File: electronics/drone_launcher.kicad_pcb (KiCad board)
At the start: 2 copper layers, 21 parts, among them J1 Servos F1, J10 I2C IMU, J11 I2C GPS, J12 I2C LCD, J13 BTNS F1R1, J14 BTNS F1R2, J15 BTNS F2R1, J16 BTNS F2R2, J17 BTNS F3R1, J18 BTNS F3R2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

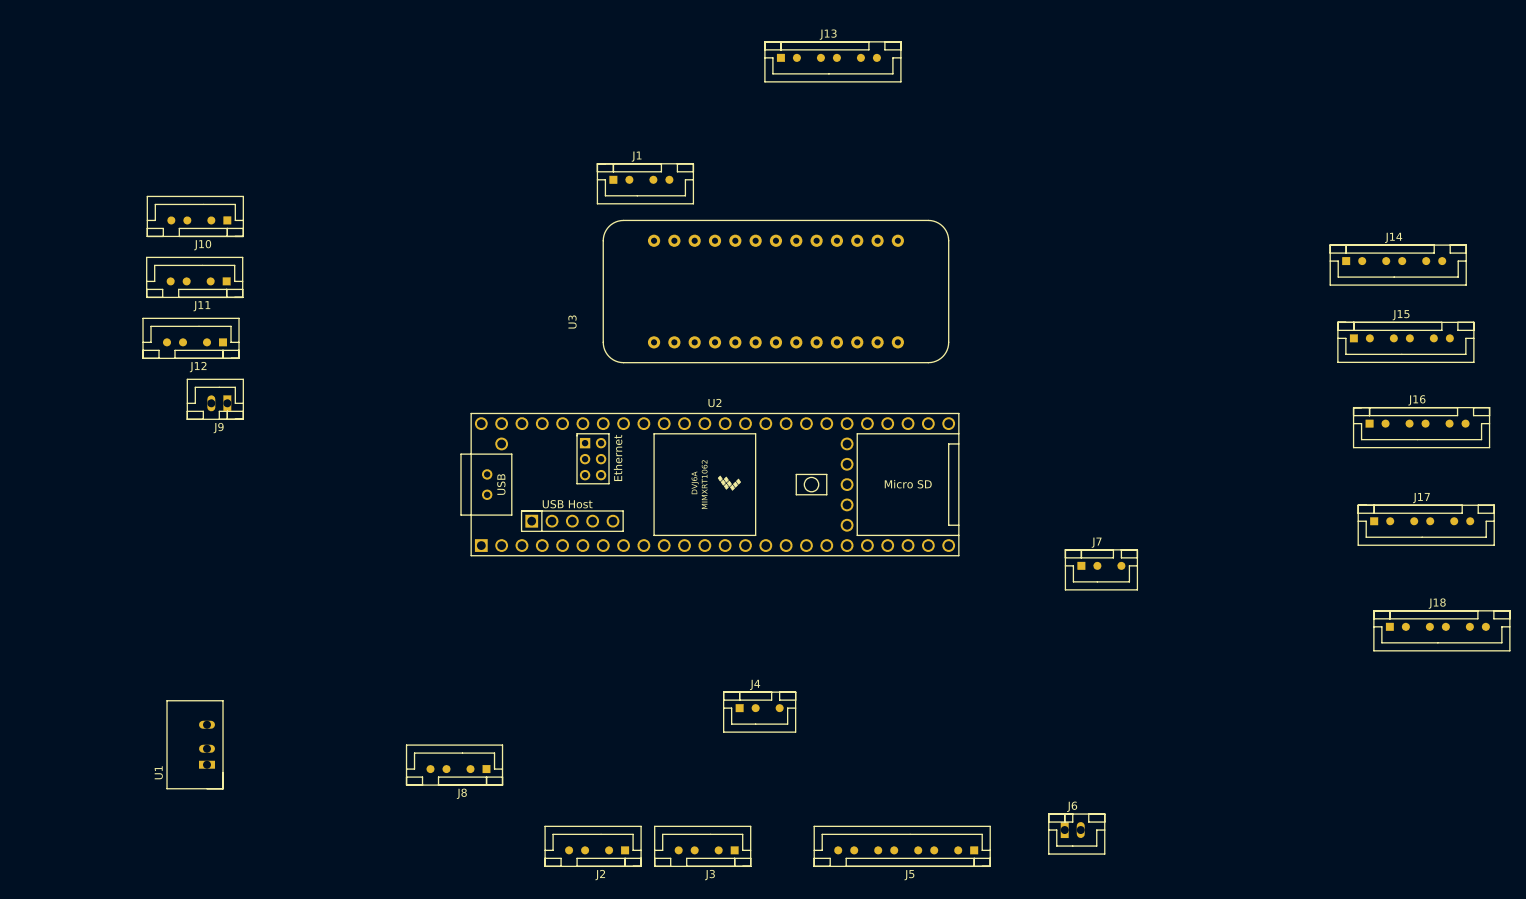
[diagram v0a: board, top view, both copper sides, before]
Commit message: improved routing and new footprints
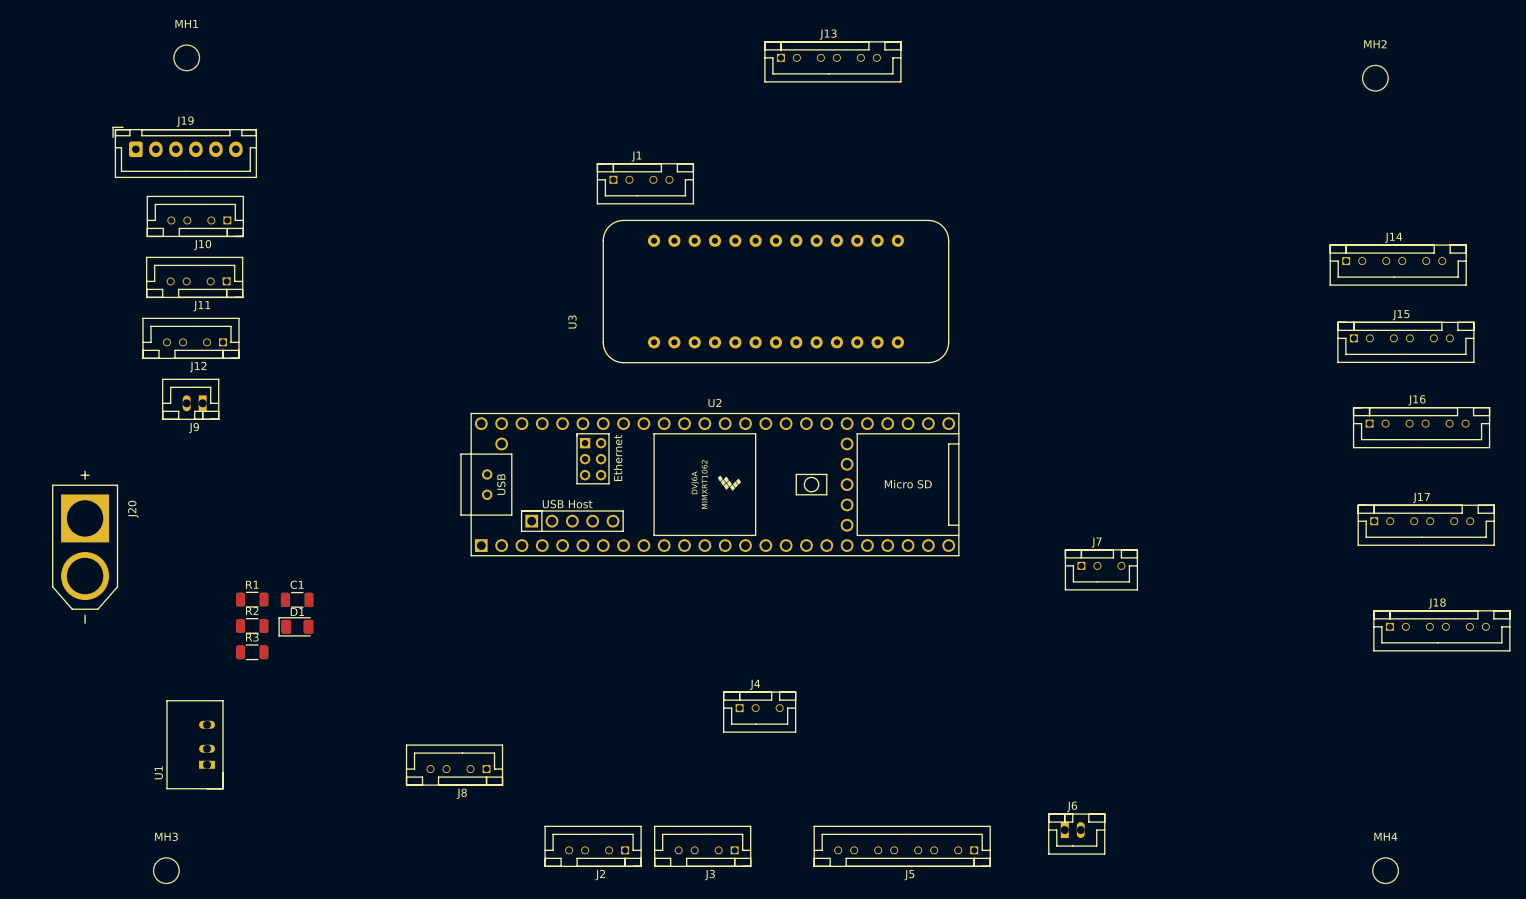
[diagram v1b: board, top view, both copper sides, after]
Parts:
- added C1: 2u2, Capacitor_SMD:C_1206_3216Metric, F.Cu at (123.0, 103.3)
- added D1: RED, LED_SMD:LED_1206_3216Metric, F.Cu at (123.1, 106.7)
- added J19: GPS, Connector_JST:JST_XH_B6B-XH-A_1x06_P2.50mm_Vertical, F.Cu at (102.9, 47.0)
- added J20: XT60-M, Connector_XT60:AMASS_XT60-M, F.Cu at (96.5, 96.7)
- added MH1: ~, MountingHole:MountingHole_3.2mm_M3, F.Cu at (109.2, 35.6)
- added MH2: ~, MountingHole:MountingHole_3.2mm_M3, F.Cu at (257.8, 38.1)
- added MH3: ~, MountingHole:MountingHole_3.2mm_M3, F.Cu at (106.7, 137.2)
- added MH4: ~, MountingHole:MountingHole_3.2mm_M3, F.Cu at (259.1, 137.2)
- added R1: 800M, Resistor_SMD:R_1206_3216Metric, F.Cu at (117.4, 103.3)
- added R2: 100M, Resistor_SMD:R_1206_3216Metric, F.Cu at (117.4, 106.6)
- added R3: 1k, Resistor_SMD:R_1206_3216Metric, F.Cu at (117.4, 109.9)
- J11: value I2C GPS -> I2C LCD
- J12: value I2C LCD -> I2C Extra
- moved J9 3.08 mm to (111.2, 78.7)
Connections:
- J10 pad 1: /SDA -> +5V
- J10 pad 2: /SCL -> /SDA
- J10 pad 3: GND -> /SCL
- J10 pad 4: +5V -> GND
- J11 pad 1: /SDA -> +5V
- J11 pad 2: /SCL -> /SDA
- J11 pad 3: GND -> /SCL
- J11 pad 4: +5V -> GND
- J12 pad 1: /SDA -> +5V
- J12 pad 2: /SCL -> /SDA
- J12 pad 3: GND -> /SCL
- J12 pad 4: +5V -> GND
- U2 pad 10: /F3R1_SAFETY_SERVO -> /F2R1_SAFETY_SERVO
- U2 pad 11: /F3R2_SAFETY_SERVO -> /F2R2_SAFETY_SERVO
- U2 pad 12: unconnected-(U2-10_CS_MQSR-Pad12) -> /F3R1_TRIGGER_SERVO
- U2 pad 13: unconnected-(U2-11_MOSI_CTX1-Pad13) -> /F3R2_TRIGGER_SERVO
- U2 pad 14: unconnected-(U2-12_MISO_MQSL-Pad14) -> /F3R1_SAFETY_SERVO
- U2 pad 16: /BAT_MEAS -> /F3R2_SAFETY_SERVO
- U2 pad 26: /F1R1_SAFETY_SW -> /F3R2_BOTM_SW
- U2 pad 27: /F1R1_TOP_SW -> /F3R2_SAFETY_SW
- U2 pad 34: unconnected-(U2-GND-Pad34) -> GND
- U2 pad 36: /F1R1_TRIGGER_SERVO -> unconnected-(U2-14_A0_TX3_SPDIF_OUT-Pad36)
- U2 pad 37: /F1R2_TRIGGER_SERVO -> unconnected-(U2-15_A1_RX3_SPDIF_IN-Pad37)
- U2 pad 38: unconnected-(U2-16_A2_RX4_SCL1-Pad38) -> /GPS_RX
- U2 pad 39: unconnected-(U2-17_A3_TX4_SDA1-Pad39) -> /GPS_TX
- U2 pad 4: /F2R1_TRIGGER_SERVO -> /F1R1_TRIGGER_SERVO
- U2 pad 44: /F1R1_SAFETY_SERVO -> unconnected-(U2-22_A8_CTX1-Pad44)
- U2 pad 45: /F1R2_SAFETY_SERVO -> /BAT_MEAS
- U2 pad 5: /F2R2_TRIGGER_SERVO -> /F1R2_TRIGGER_SERVO
- U2 pad 6: /F2R1_SAFETY_SERVO -> /F1R1_SAFETY_SERVO
- U2 pad 7: /F2R2_SAFETY_SERVO -> /F1R2_SAFETY_SERVO
- U2 pad 8: /F3R1_TRIGGER_SERVO -> /F2R1_TRIGGER_SERVO
- U2 pad 9: /F3R2_TRIGGER_SERVO -> /F2R2_TRIGGER_SERVO
- U3 pad 1: GND -> +5V
- U3 pad 10: /F3R1_SAFETY_SW -> /F2R2_BOTM_SW
- U3 pad 11: /F3R1_TOP_SW -> /F2R2_SAFETY_SW
- U3 pad 12: /F2R2_BOTM_SW -> /F2R2_TOP_SW
- U3 pad 13: /F2R2_SAFETY_SW -> /F2R1_BOTM_SW
- U3 pad 19: /F1R1_BOTM_SW -> /F1R1_TOP_SW
- U3 pad 2: (no net) -> GND
- U3 pad 20: /F1R2_TOP_SW -> /F1R1_SAFETY_SW
- U3 pad 21: /F1R2_SAFETY_SW -> /F1R1_BOTM_SW
- U3 pad 22: /F1R2_BOTM_SW -> /F1R2_TOP_SW
- U3 pad 23: /F2_R1_TOP_SW -> /F1R2_SAFETY_SW
- U3 pad 24: /F2R1_SAFETY_SW -> /F1R2_BOTM_SW
- U3 pad 25: /F2R1_BOTM_SW -> /F2_R1_TOP_SW
- U3 pad 26: /F2R2_TOP_SW -> /F2R1_SAFETY_SW
- U3 pad 6: /F3R2_BOTM_SW -> /F3R2_TOP_SW
- U3 pad 7: /F3R2_SAFETY_SW -> /F3R1_BOTM_SW
- U3 pad 8: /F3R2_TOP_SW -> /F3R1_SAFETY_SW
- U3 pad 9: /F3R1_BOTM_SW -> /F3R1_TOP_SW

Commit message: version 1.0 pcb
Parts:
- removed J12: I2C Extra, Connector_JST:JST_XH_B4B-XH-A_1x04_P2.50mm_Vertical
- added D4: RED, LED_SMD:LED_1206_3216Metric, F.Cu at (181.4, 105.3)
- added D5: GREEN, LED_SMD:LED_1206_3216Metric, F.Cu at (185.2, 105.3)
- added G***: LOGO, LOGO, F.Cu at (149.1, 119.1)
- added R6: 1k, Resistor_SMD:R_1206_3216Metric, F.Cu at (181.4, 110.4)
- added R7: 1k, Resistor_SMD:R_1206_3216Metric, F.Cu at (185.2, 110.4)
- C1: value 2u2 -> 220n
- J20: value XT60-M -> PWR IN
- R1: value 800M -> 820K
- R2: value 100M -> 120K
- moved J14 110.7 mm to (143.5, 64.0)
- moved J1 92.5 mm to (113.9, 129.5), turned to 180 degrees
- moved J15 91.9 mm to (163.4, 64.0)
- moved J16 75.6 mm to (183.5, 64.0)
- moved J13 66.3 mm to (123.6, 64.0)
- moved J19 65.4 mm to (96.1, 112.0)
- moved MH2 60.0 mm to (203.6, 63.7)
- moved J17 58.4 mm to (203.5, 71.7), turned to -90 degrees
- moved J18 57.8 mm to (203.2, 94.1), turned to -90 degrees
- moved MH4 56.0 mm to (203.6, 129.7)
- moved J8 50.8 mm to (96.1, 120.1), turned to 0 degrees
- moved U1 43.3 mm to (115.1, 80.8), turned to 0 degrees
- moved J2 35.5 mm to (128.9, 129.5)
- moved J11 34.6 mm to (96.0, 93.0), turned to 0 degrees
- moved J10 34.1 mm to (95.8, 84.6), turned to 0 degrees
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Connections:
- J19 pad 2: /SDA -> /GPS_RX
- J19 pad 3: /SCL -> /GPS_TX
- J19 pad 4: /GPS_RX -> /SDA
- J19 pad 5: /GPS_TX -> /SCL
- U2 pad 28: unconnected-(U2-36_CS-Pad28) -> /LED_ALIVE
- U2 pad 29: unconnected-(U2-37_CS-Pad29) -> /LED_DBG
- U2 pad 36: unconnected-(U2-14_A0_TX3_SPDIF_OUT-Pad36) -> /RST_MCP
- U2 pad 38: /GPS_RX -> unconnected-(U2-16_A2_RX4_SCL1-Pad38)
- U2 pad 39: /GPS_TX -> unconnected-(U2-17_A3_TX4_SDA1-Pad39)
- U2 pad 42: unconnected-(U2-20_A6_TX5_LRCLK1-Pad42) -> /GPS_TX
- U2 pad 43: unconnected-(U2-21_A7_RX5_BCLK1-Pad43) -> /GPS_RX
- U3 pad 10: /F2R2_BOTM_SW -> /F3R1_TOP_SW
- U3 pad 11: /F2R2_SAFETY_SW -> /F3R1_SAFETY_SW
- U3 pad 12: /F2R2_TOP_SW -> /F3R1_BOTM_SW
- U3 pad 13: /F2R1_BOTM_SW -> /F3R2_TOP_SW
- U3 pad 5: unconnected-(U3-RST-Pad5) -> /RST_MCP
- U3 pad 6: /F3R2_TOP_SW -> /F2R1_BOTM_SW
- U3 pad 7: /F3R1_BOTM_SW -> /F2R2_TOP_SW
- U3 pad 8: /F3R1_SAFETY_SW -> /F2R2_SAFETY_SW
- U3 pad 9: /F3R1_TOP_SW -> /F2R2_BOTM_SW
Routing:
- net +5V: track 0.00 -> 209.1 mm, vias 0 -> 4
- net /SDA: track 0.00 -> 98.4 mm, vias 0 -> 4
- net /SCL: track 0.00 -> 94.9 mm, vias 0 -> 2
- net /SPI_SCK: track 0.00 -> 76.2 mm
- net /SPI_MOSI: track 0.00 -> 70.0 mm
- net /GPS_RX: track 0.00 -> 44.6 mm
- net /GPS_TX: track 0.00 -> 43.7 mm
- net /F2R2_BOTM_SW: track 0.00 -> 43.0 mm
- net /F3R1_TOP_SW: track 0.00 -> 42.9 mm
- net /F2R2_SAFETY_SW: track 0.00 -> 41.8 mm
- net /F2R2_TOP_SW: track 0.00 -> 40.0 mm
- net /F1R1_TOP_SW: track 0.00 -> 39.9 mm
- net /F2R1_BOTM_SW: track 0.00 -> 39.4 mm
- net /F3R1_SAFETY_SW: track 0.00 -> 38.3 mm
- net /LEDS_DRONE: track 0.00 -> 37.5 mm
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- added copper zone on F.Cu, net +24V
- added copper zone on F.Cu, net +5V
- added copper zone on B.Cu, net GND
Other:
- board outline added: 117.9 x 75.7 mm
- board text added: "ARM SW"
- board text added: "BTNS F1R1"
- board text added: "BTNS F1R2"
- board text added: "BTNS F2R1"
- board text added: "BTNS F2R2"
- board text added: "BTNS F3R1"
- board text added: "BTNS F3R2"
- board text added: "COM"
- board text added: "Drone Launcher Controller V1.0"
- board text added: "GPS"
- board text added: "IMU"
- board text added: "LCD"
- board text added: "LED BAT"
- board text added: "LED DRONE"
- board text added: "MENU BTNS"
- board text added: "PWR IN"
- board text added: "SERVO F1"
- board text added: "SERVO F2"
- board text added: "SERVO F3"
- board text added: "SPI"
